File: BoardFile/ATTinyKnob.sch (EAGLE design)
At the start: 14 parts, among them U1 ATTINY_25_45_85

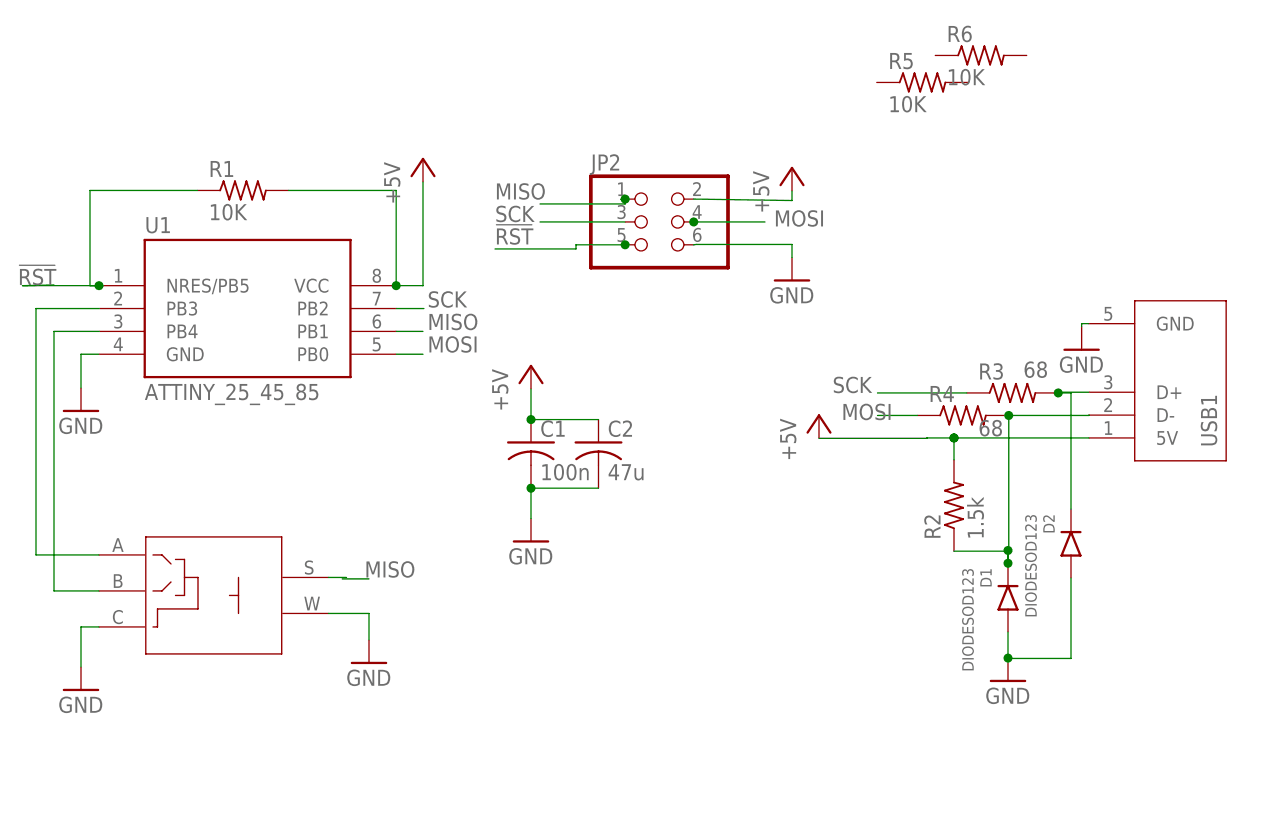
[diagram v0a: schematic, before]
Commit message: Created board, added 3d files
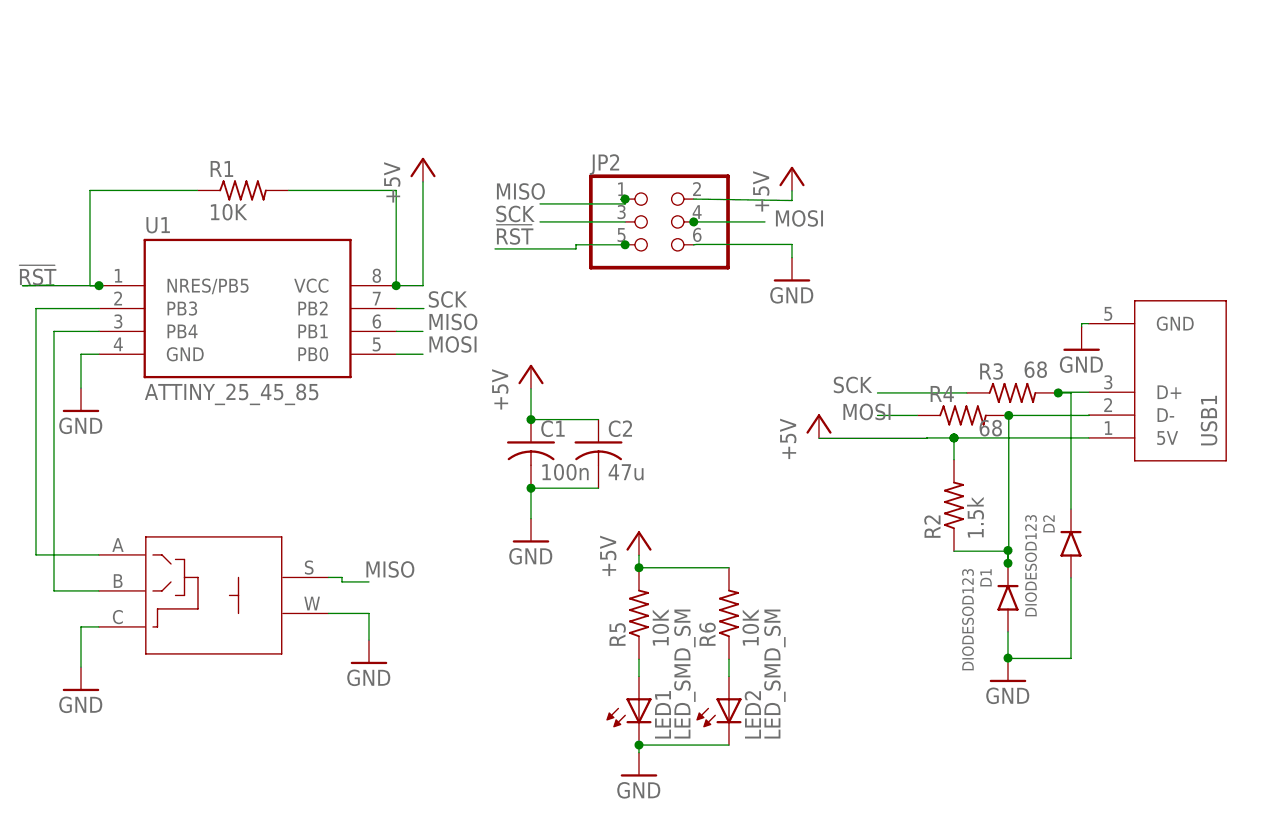
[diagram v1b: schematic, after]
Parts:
- added LED1, LED2: LED_SMD_SM, DR:LED_SMD_SM
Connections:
- removed net N$10: ROT1.S
- new net N$7: LED2.A, R6.1
- new net N$8: LED1.A, R5.1
- net +5V: now also R5.2, R6.2
- net GND: now also LED1.C, LED2.C
- net MISO: now also ROT1.S
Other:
- moved on the sheet: R5, R6
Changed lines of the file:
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@@
 <part name="P+4" library="supply1" library_urn="urn:adsk.eagle:library:371" deviceset="+5V" device=""/>
 <part name="GND5" library="supply1" library_urn="urn:adsk.eagle:library:371" deviceset="GND" device=""/>
+<part name="LED1" library="DR" deviceset="LED_SMD_SM" device=""/>
+<part name="LED2" library="DR" deviceset="LED_SMD_SM" device=""/>
+<part name="P+5" library="supply1" library_urn="urn:adsk.eagle:library:371" deviceset="+5V" device=""/>
+<part name="GND8" library="supply1" library_urn="urn:adsk.eagle:library:371" deviceset="GND" device=""/>
 </parts>
 <sheets>
@@
 <attribute name="VALUE" x="117.69" y="93.198" size="1.778" layer="96"/>
 </instance>
-<instance part="R5" gate="G$1" x="111.5" y="132.5" smashed="yes">
-<attribute name="NAME" x="107.69" y="133.9986" size="1.778" layer="95"/>
-<attribute name="VALUE" x="107.69" y="129.198" size="1.778" layer="96"/>
-</instance>
-<instance part="R6" gate="G$1" x="118" y="135.5" smashed="yes">
-<attribute name="NAME" x="114.19" y="136.9986" size="1.778" layer="95"/>
-<attribute name="VALUE" x="114.19" y="132.198" size="1.778" layer="96"/>
+<instance part="R5" gate="G$1" x="80" y="73.5" smashed="yes" rot="R90">
+<attribute name="NAME" x="78.5014" y="69.69" size="1.778" layer="95" rot="R90"/>
+<attribute name="VALUE" x="83.302" y="69.69" size="1.778" layer="96" rot="R90"/>
+</instance>
+<instance part="R6" gate="G$1" x="90" y="73.5" smashed="yes" rot="R90">
+<attribute name="NAME" x="88.5014" y="69.69" size="1.778" layer="95" rot="R90"/>
+<attribute name="VALUE" x="93.302" y="69.69" size="1.778" layer="96" rot="R90"/>
 </instance>
 <instance part="P+2" gate="1" x="100" y="95.5" smashed="yes">
@@
 <instance part="GND5" gate="1" x="97" y="110.5" smashed="yes">
 <attribute name="VALUE" x="94.46" y="107.96" size="1.778" layer="96"/>
+</instance>
+<instance part="LED1" gate="G$1" x="80" y="66.5" smashed="yes">
+<attribute name="NAME" x="83.556" y="59.388" size="1.778" layer="95" rot="R90"/>
+<attribute name="VALUE" x="85.715" y="59.388" size="1.778" layer="96" rot="R90"/>
+</instance>
+<instance part="LED2" gate="G$1" x="90" y="66.5" smashed="yes">
+<attribute name="NAME" x="93.556" y="59.388" size="1.778" layer="95" rot="R90"/>
+<attribute name="VALUE" x="95.715" y="59.388" size="1.778" layer="96" rot="R90"/>
+</instance>
+<instance part="P+5" gate="1" x="80" y="82.5" smashed="yes">
+<attribute name="VALUE" x="77.46" y="77.42" size="1.778" layer="96" rot="R90"/>
+</instance>
+<instance part="GND8" gate="1" x="80" y="55.5" smashed="yes">
+<attribute name="VALUE" x="77.46" y="52.96" size="1.778" layer="96"/>
 </instance>
 </instances>
@@
 <wire x1="97" y1="114.5" x2="86.36" y2="114.5" width="0.1524" layer="91"/>
 <wire x1="86.36" y1="114.5" x2="86.08" y2="114.46" width="0.1524" layer="91"/>
+</segment>
+<segment>
+<pinref part="LED2" gate="G$1" pin="C"/>
+<pinref part="LED1" gate="G$1" pin="C"/>
+<wire x1="90" y1="58.88" x2="80" y2="58.88" width="0.1524" layer="91"/>
+<pinref part="GND8" gate="1" pin="GND"/>
+<wire x1="80" y1="58.04" x2="80" y2="58.88" width="0.1524" layer="91"/>
+<junction x="80" y="58.88"/>
 </segment>
 </net>
@@
 <junction x="115" y="93"/>
 </segment>
+<segment>
+<pinref part="R5" gate="G$1" pin="2"/>
+<pinref part="P+5" gate="1" pin="+5V"/>
+<wire x1="80" y1="78.58" x2="80" y2="79.96" width="0.1524" layer="91"/>
+<pinref part="R6" gate="G$1" pin="2"/>
+<wire x1="90" y1="78.58" x2="80" y2="78.58" width="0.1524" layer="91"/>
+<junction x="80" y="78.58"/>
+</segment>
 </net>
 <net name="SCK" class="0">
@@
 </segment>
 <segment>
-<wire x1="47.02" y1="77.34" x2="50" y2="77.34" width="0.1524" layer="91"/>
+<wire x1="47" y1="77" x2="50" y2="77" width="0.1524" layer="91"/>
 <label x="49.5" y="77.5" size="1.778" layer="95"/>
+<wire x1="47" y1="77" x2="47" y2="77.5" width="0.1524" layer="91"/>
+<pinref part="ROT1" gate="G$1" pin="S"/>
+<wire x1="47" y1="77.5" x2="45.5" y2="77.5" width="0.1524" layer="91"/>
 </segment>
 <segment>
@@
 </segment>
 </net>
-<net name="N$10" class="0">
-<segment>
-<pinref part="ROT1" gate="G$1" pin="S"/>
-<wire x1="47.5" y1="77.5" x2="45.5" y2="77.5" width="0.1524" layer="91"/>
-</segment>
-</net>
 <net name="N$3" class="0">
 <segment>
@@
 </segment>
 </net>
+<net name="N$7" class="0">
+<segment>
+<pinref part="LED2" gate="G$1" pin="A"/>
+<pinref part="R6" gate="G$1" pin="1"/>
+<wire x1="90" y1="66.5" x2="90" y2="68.42" width="0.1524" layer="91"/>
+</segment>
+</net>
+<net name="N$8" class="0">
+<segment>
+<pinref part="LED1" gate="G$1" pin="A"/>
+<pinref part="R5" gate="G$1" pin="1"/>
+<wire x1="80" y1="66.5" x2="80" y2="68.42" width="0.1524" layer="91"/>
+</segment>
+</net>

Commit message: Added through hole usb
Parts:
- USB1: value USB_MINI -> USB_MINIUSB_MINI_TH_RIGHTANG; device DR:USB_MINI -> DR:USB_MINIUSB_MINI_TH_RIGHTANG
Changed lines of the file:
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@@
 <part name="U1" library="DR" deviceset="ATTINY_25_45_85" device=""/>
 <part name="JP2" library="pinhead" library_urn="urn:adsk.eagle:library:325" deviceset="PINHD-2X3" device="" package3d_urn="urn:adsk.eagle:package:22462/2"/>
-<part name="USB1" library="DR" deviceset="USB_MINI" device=""/>
 <part name="GND6" library="supply1" library_urn="urn:adsk.eagle:library:371" deviceset="GND" device=""/>
 <part name="GND7" library="supply1" library_urn="urn:adsk.eagle:library:371" deviceset="GND" device=""/>
@@
 <part name="P+5" library="supply1" library_urn="urn:adsk.eagle:library:371" deviceset="+5V" device=""/>
 <part name="GND8" library="supply1" library_urn="urn:adsk.eagle:library:371" deviceset="GND" device=""/>
+<part name="USB1" library="DR" deviceset="USB_MINI" device="USB_MINI_TH_RIGHTANG"/>
 </parts>
 <sheets>
@@
 <attribute name="VALUE" x="74.65" y="109.38" size="1.778" layer="96"/>
 </instance>
-<instance part="USB1" gate="G$1" x="130" y="93" smashed="yes" rot="R90">
-<attribute name="NAME" x="144.224" y="91.984" size="1.778" layer="95" rot="R90"/>
-</instance>
 <instance part="GND6" gate="1" x="18" y="96" smashed="yes">
 <attribute name="VALUE" x="15.46" y="93.46" size="1.778" layer="96"/>
@@
 <instance part="GND8" gate="1" x="80" y="55.5" smashed="yes">
 <attribute name="VALUE" x="77.46" y="52.96" size="1.778" layer="96"/>
+</instance>
+<instance part="USB1" gate="G$1" x="132" y="93" smashed="yes" rot="R90">
+<attribute name="NAME" x="146.224" y="91.984" size="1.778" layer="95" rot="R90"/>
 </instance>
 </instances>
@@
 <pinref part="GND1" gate="1" pin="GND"/>
 <wire x1="18" y1="72" x2="18" y2="67.54" width="0.1524" layer="91"/>
-</segment>
-<segment>
-<pinref part="USB1" gate="G$1" pin="GND"/>
-<pinref part="GND7" gate="1" pin="GND"/>
-<wire x1="130" y1="105.7" x2="129.18" y2="105.7" width="0.1524" layer="91"/>
-<wire x1="129.18" y1="105.7" x2="129.18" y2="105.34" width="0.1524" layer="91"/>
 </segment>
 <segment>
@@
 <wire x1="80" y1="58.04" x2="80" y2="58.88" width="0.1524" layer="91"/>
 <junction x="80" y="58.88"/>
+</segment>
+<segment>
+<pinref part="USB1" gate="G$1" pin="GND"/>
+<pinref part="GND7" gate="1" pin="GND"/>
+<wire x1="132" y1="105.7" x2="129.18" y2="105.7" width="0.1524" layer="91"/>
+<wire x1="129.18" y1="105.7" x2="129.18" y2="105.34" width="0.1524" layer="91"/>
 </segment>
 </net>
@@
 </segment>
 <segment>
-<pinref part="USB1" gate="G$1" pin="5V"/>
-<wire x1="130" y1="93" x2="115" y2="93" width="0.1524" layer="91"/>
+<wire x1="132" y1="93" x2="115" y2="93" width="0.1524" layer="91"/>
 <pinref part="P+2" gate="1" pin="+5V"/>
 <wire x1="115" y1="93" x2="112" y2="93" width="0.1524" layer="91"/>
@@
 <wire x1="115" y1="90.58" x2="115" y2="93" width="0.1524" layer="91"/>
 <junction x="115" y="93"/>
+<pinref part="USB1" gate="G$1" pin="5V"/>
 </segment>
 <segment>
@@
 <net name="N$4" class="0">
 <segment>
-<pinref part="USB1" gate="G$1" pin="D+"/>
 <pinref part="R3" gate="G$1" pin="2"/>
-<wire x1="130" y1="98.08" x2="126.58" y2="98.08" width="0.1524" layer="91"/>
-<wire x1="126.58" y1="98.08" x2="126.58" y2="98" width="0.1524" layer="91"/>
 <pinref part="D2" gate="G$1" pin="C"/>
 <wire x1="128" y1="85.08" x2="128" y2="98" width="0.1524" layer="91"/>
 <wire x1="128" y1="98" x2="126.58" y2="98" width="0.1524" layer="91"/>
 <junction x="126.58" y="98"/>
+<pinref part="USB1" gate="G$1" pin="D+"/>
+<wire x1="132" y1="98.08" x2="126.58" y2="98.08" width="0.1524" layer="91"/>
+<wire x1="126.58" y1="98.08" x2="126.58" y2="98" width="0.1524" layer="91"/>
 </segment>
 </net>
 <net name="N$6" class="0">
 <segment>
-<pinref part="USB1" gate="G$1" pin="D-"/>
 <pinref part="R4" gate="G$1" pin="2"/>
-<wire x1="130" y1="95.54" x2="130" y2="95.5" width="0.1524" layer="91"/>
 <wire x1="130" y1="95.5" x2="121.08" y2="95.5" width="0.1524" layer="91"/>
 <wire x1="121.08" y1="95.5" x2="121.08" y2="80.5" width="0.1524" layer="91"/>
@@
 <wire x1="121" y1="80.42" x2="121" y2="79.08" width="0.1524" layer="91"/>
 <junction x="121" y="79.08"/>
-</segment>
-</net>
+<pinref part="USB1" gate="G$1" pin="D-"/>
+<wire x1="130" y1="95.5" x2="130" y2="95.54" width="0.1524" layer="91"/>
+<wire x1="130" y1="95.54" x2="132" y2="95.54" width="0.1524" layer="91"/>
+</segment>
+</net>

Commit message: Board built
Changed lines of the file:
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@@
 <attribute name="VALUE" x="126.64" y="100.26" size="1.778" layer="96"/>
 </instance>
-<instance part="P+1" gate="1" x="56" y="124" smashed="yes">
-<attribute name="VALUE" x="53.46" y="118.92" size="1.778" layer="96" rot="R90"/>
+<instance part="P+1" gate="1" x="58.5" y="118" smashed="yes">
+<attribute name="VALUE" x="55.96" y="112.92" size="1.778" layer="96" rot="R90"/>
 </instance>
 <instance part="ROT1" gate="G$1" x="20" y="80" smashed="yes">
@@
 <net name="+5V" class="0">
 <segment>
+<pinref part="P+1" gate="1" pin="+5V"/>
+<wire x1="58.5" y1="109.92" x2="58.5" y2="115.46" width="0.1524" layer="91"/>
 <pinref part="U1" gate="G$1" pin="VCC"/>
-<pinref part="P+1" gate="1" pin="+5V"/>
-<wire x1="53.02" y1="109.92" x2="56" y2="109.92" width="0.1524" layer="91"/>
-<wire x1="56" y1="109.92" x2="56" y2="121.46" width="0.1524" layer="91"/>
+<wire x1="53.02" y1="109.92" x2="58.5" y2="109.92" width="0.1524" layer="91"/>
 <pinref part="R1" gate="G$1" pin="2"/>
-<wire x1="41.08" y1="120.5" x2="52.5" y2="120.5" width="0.1524" layer="91"/>
-<wire x1="52.5" y1="120.5" x2="53.02" y2="120.5" width="0.1524" layer="91"/>
-<wire x1="53.02" y1="120.5" x2="53.02" y2="109.92" width="0.1524" layer="91"/>
+<wire x1="41.08" y1="120.5" x2="55.5" y2="120.5" width="0.1524" layer="91"/>
+<wire x1="55.5" y1="120.5" x2="55.52" y2="120.5" width="0.1524" layer="91"/>
+<wire x1="55.5" y1="120.5" x2="55.5" y2="109.92" width="0.1524" layer="91"/>
+<wire x1="55.5" y1="109.92" x2="53.02" y2="109.92" width="0.1524" layer="91"/>
+<junction x="55.5" y="120.5"/>
 <junction x="53.02" y="109.92"/>
 </segment>
@@
 </segment>
 <segment>
+<pinref part="P+2" gate="1" pin="+5V"/>
+<pinref part="USB1" gate="G$1" pin="5V"/>
+<pinref part="R2" gate="G$1" pin="2"/>
 <wire x1="132" y1="93" x2="115" y2="93" width="0.1524" layer="91"/>
-<pinref part="P+2" gate="1" pin="+5V"/>
-<wire x1="115" y1="93" x2="112" y2="93" width="0.1524" layer="91"/>
-<wire x1="112" y1="93" x2="112" y2="92.96" width="0.1524" layer="91"/>
-<wire x1="112" y1="92.96" x2="100" y2="92.96" width="0.1524" layer="91"/>
-<pinref part="R2" gate="G$1" pin="2"/>
-<wire x1="115" y1="90.58" x2="115" y2="93" width="0.1524" layer="91"/>
+<wire x1="115" y1="93" x2="115" y2="90.58" width="0.1524" layer="91"/>
+<wire x1="115" y1="93" x2="100" y2="93" width="0.1524" layer="91"/>
+<wire x1="100" y1="93" x2="100" y2="92.96" width="0.1524" layer="91"/>
 <junction x="115" y="93"/>
-<pinref part="USB1" gate="G$1" pin="5V"/>
 </segment>
 <segment>
@@
 </segment>
 </net>
-<net name="N$3" class="0">
-<segment>
-<junction x="115" y="93"/>
-</segment>
-</net>
 <net name="N$7" class="0">
 <segment>
@@
 </segment>
 </net>
+<net name="N$5" class="0">
+<segment>
+<wire x1="112" y1="93" x2="112" y2="92.96" width="0.1524" layer="91"/>
+</segment>
+</net>
 </nets>
 </sheet>
 </sheets>
-<errors>
-</errors>
 </schematic>
 </drawing>
